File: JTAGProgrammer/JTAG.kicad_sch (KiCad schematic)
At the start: 27 parts, among them J2 878325623, J3 Conn_01x06, U4 74LVC3G17, U5 74LVC3G17

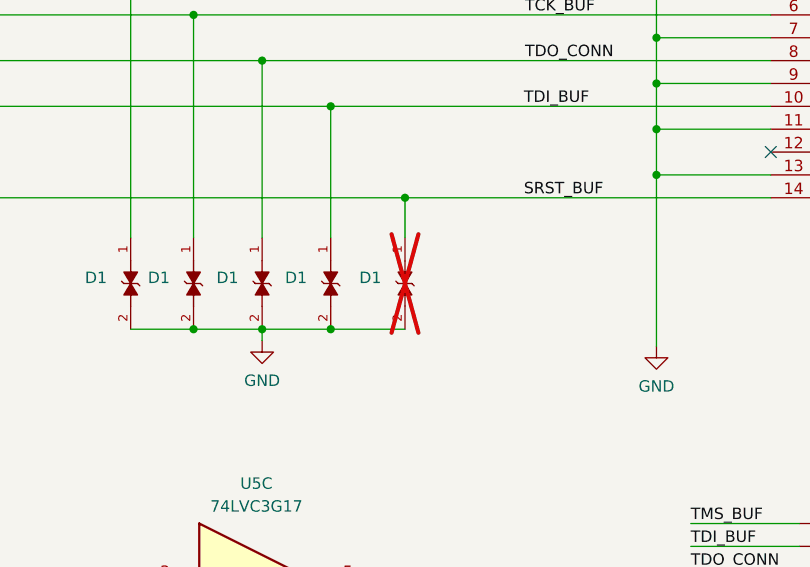
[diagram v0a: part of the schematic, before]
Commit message: Add LCSC part numbers
Signed-off-by: Anthony Bernaert <anthony.bernaert@gmail.com>
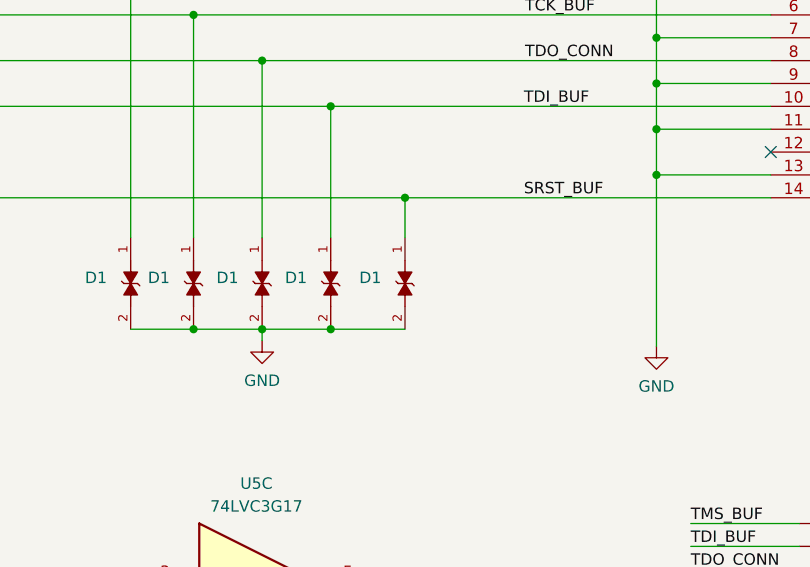
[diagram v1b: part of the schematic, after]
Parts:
- D1: LCSC (none) -> C142698
- D1: LCSC (none) -> C142698; now fitted; now in the parts list
- D4: LCSC (none) -> C324473
- J2: LCSC (none) -> C5197958
- J3: LCSC (none) -> C40877
- U4, U5: LCSC (none) -> C18213
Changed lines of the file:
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@@
+      (effects (font (size 1.27 1.27)) hide)
+    )
+    (property "LCSC" "C18213" (at 88.265 66.675 0)
       (effects (font (size 1.27 1.27)) hide)
     )
@@
     (property "Datasheet" "878325623" (at 237.49 47.625 0)
       (effects (font (size 1.27 1.27) italic) hide)
+    )
+    (property "LCSC" "C5197958" (at 237.49 47.625 0)
+      (effects (font (size 1.27 1.27)) hide)
     )
     (pin "1")
@@
       (effects (font (size 1.27 1.27)) hide)
     )
+    (property "LCSC" "C324473" (at 48.895 170.18 0)
+      (effects (font (size 1.27 1.27)) hide)
+    )
     (pin "1")
     (pin "2")
@@
     )
     (property "Datasheet" "http://www.ti.com/lit/sg/scyt129e/scyt129e.pdf" (at 87.63 104.14 0)
+      (effects (font (size 1.27 1.27)) hide)
+    )
+    (property "LCSC" "C18213" (at 87.63 104.14 0)
       (effects (font (size 1.27 1.27)) hide)
     )
@@
       (effects (font (size 1.27 1.27)) (justify bottom) hide)
     )
+    (property "LCSC" "C142698" (at 180.975 90.17 90)
+      (effects (font (size 1.27 1.27)) hide)
+    )
     (pin "1")
     (pin "2")
@@
     )
     (property "Datasheet" "http://www.ti.com/lit/sg/scyt129e/scyt129e.pdf" (at 87.63 121.92 0)
+      (effects (font (size 1.27 1.27)) hide)
+    )
+    (property "LCSC" "C18213" (at 87.63 121.92 0)
       (effects (font (size 1.27 1.27)) hide)
     )
@@
       (effects (font (size 1.27 1.27)) hide)
     )
+    (property "LCSC" "C18213" (at 85.725 83.82 0)
+      (effects (font (size 1.27 1.27)) hide)
+    )
     (pin "1")
     (pin "7")
@@
       (effects (font (size 1.27 1.27)) (justify bottom) hide)
     )
+    (property "LCSC" "C142698" (at 188.595 90.17 90)
+      (effects (font (size 1.27 1.27)) hide)
+    )
     (pin "1")
     (pin "2")
@@
     )
     (property "Datasheet" "http://www.ti.com/lit/sg/scyt129e/scyt129e.pdf" (at 88.265 48.895 0)
+      (effects (font (size 1.27 1.27)) hide)
+    )
+    (property "LCSC" "C18213" (at 88.265 48.895 0)
       (effects (font (size 1.27 1.27)) hide)
     )
@@
       (effects (font (size 1.27 1.27)) hide)
     )
+    (property "LCSC" "C18213" (at 113.03 164.465 0)
+      (effects (font (size 1.27 1.27)) hide)
+    )
     (pin "1")
     (pin "7")
@@
       (effects (font (size 1.27 1.27)) (justify bottom) hide)
     )
+    (property "LCSC" "C142698" (at 173.355 90.17 90)
+      (effects (font (size 1.27 1.27)) hide)
+    )
     (pin "1")
     (pin "2")
@@
     )
     (property "Datasheet" "http://www.ti.com/lit/sg/scyt129e/scyt129e.pdf" (at 127 164.465 0)
+      (effects (font (size 1.27 1.27)) hide)
+    )
+    (property "LCSC" "C18213" (at 127 164.465 0)
       (effects (font (size 1.27 1.27)) hide)
     )
@@
       (effects (font (size 1.27 1.27)) (justify bottom) hide)
     )
+    (property "LCSC" "C142698" (at 166.37 90.17 90)
+      (effects (font (size 1.27 1.27)) hide)
+    )
     (pin "1")
     (pin "2")
@@
     )
     (property "Datasheet" "http://www.ti.com/lit/sg/scyt129e/scyt129e.pdf" (at 181.61 123.19 0)
+      (effects (font (size 1.27 1.27)) hide)
+    )
+    (property "LCSC" "C18213" (at 181.61 123.19 0)
       (effects (font (size 1.27 1.27)) hide)
     )
@@
       (effects (font (size 1.27 1.27)) hide)
     )
+    (property "LCSC" "C40877" (at 245.745 121.92 0)
+      (effects (font (size 1.27 1.27)) hide)
+    )
     (pin "1")
     (pin "2")
@@
       (effects (font (size 1.27 1.27)) hide)
     )
+    (property "LCSC" "C324473" (at 48.895 147.955 0)
+      (effects (font (size 1.27 1.27)) hide)
+    )
     (pin "1")
     (pin "2")
@@
       (effects (font (size 1.27 1.27)) hide)
     )
+    (property "LCSC" "C324473" (at 48.26 158.75 0)
+      (effects (font (size 1.27 1.27)) hide)
+    )
     (pin "1")
     (pin "2")
@@
   )
   (symbol (lib_id "PGB1010603MR:PGB1010603MR") (at 196.85 90.17 270) (unit 1)
-    (in_bom no) (on_board yes) (dnp yes)
+    (in_bom yes) (on_board yes) (dnp no)
     (property "Reference" "D1" (at 191.77 89.535 90)
       (effects (font (size 1.27 1.27)) (justify left))
@@
       (effects (font (size 1.27 1.27)) (justify bottom) hide)
     )
-    (pin "1")
+    (property "LCSC" "C142698" (at 196.85 90.17 90)
+      (effects (font (size 1.27 1.27)) hide)
+    )
+    (pin "1")

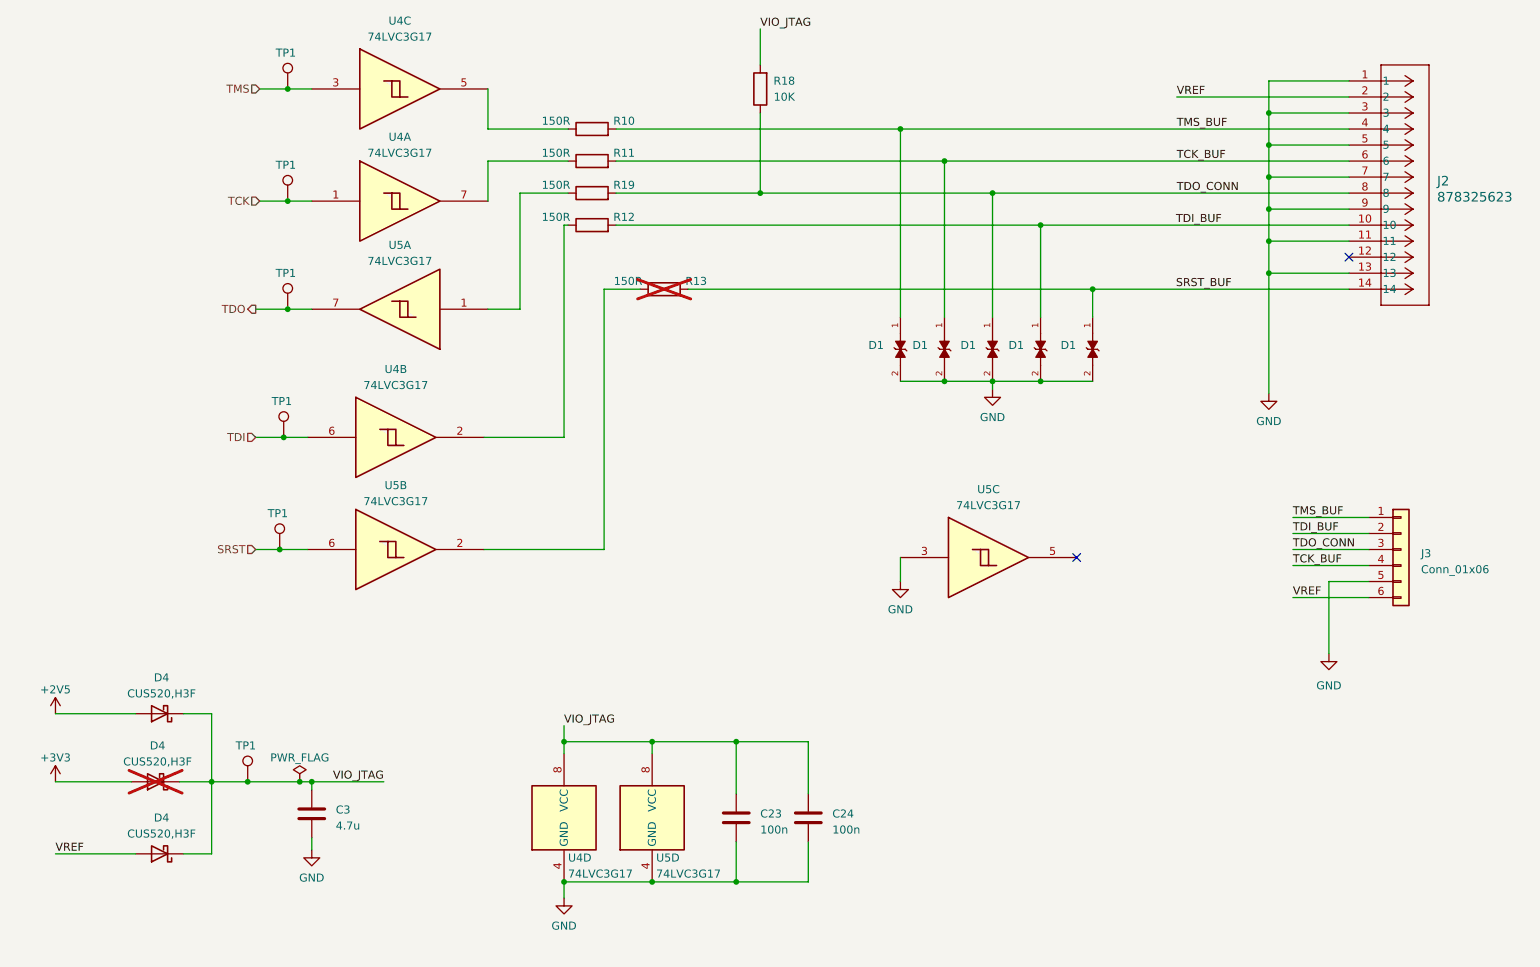
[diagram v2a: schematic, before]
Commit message: Rev.2: change to USB Type-C, add VBUS fuse, VREF LED indicators
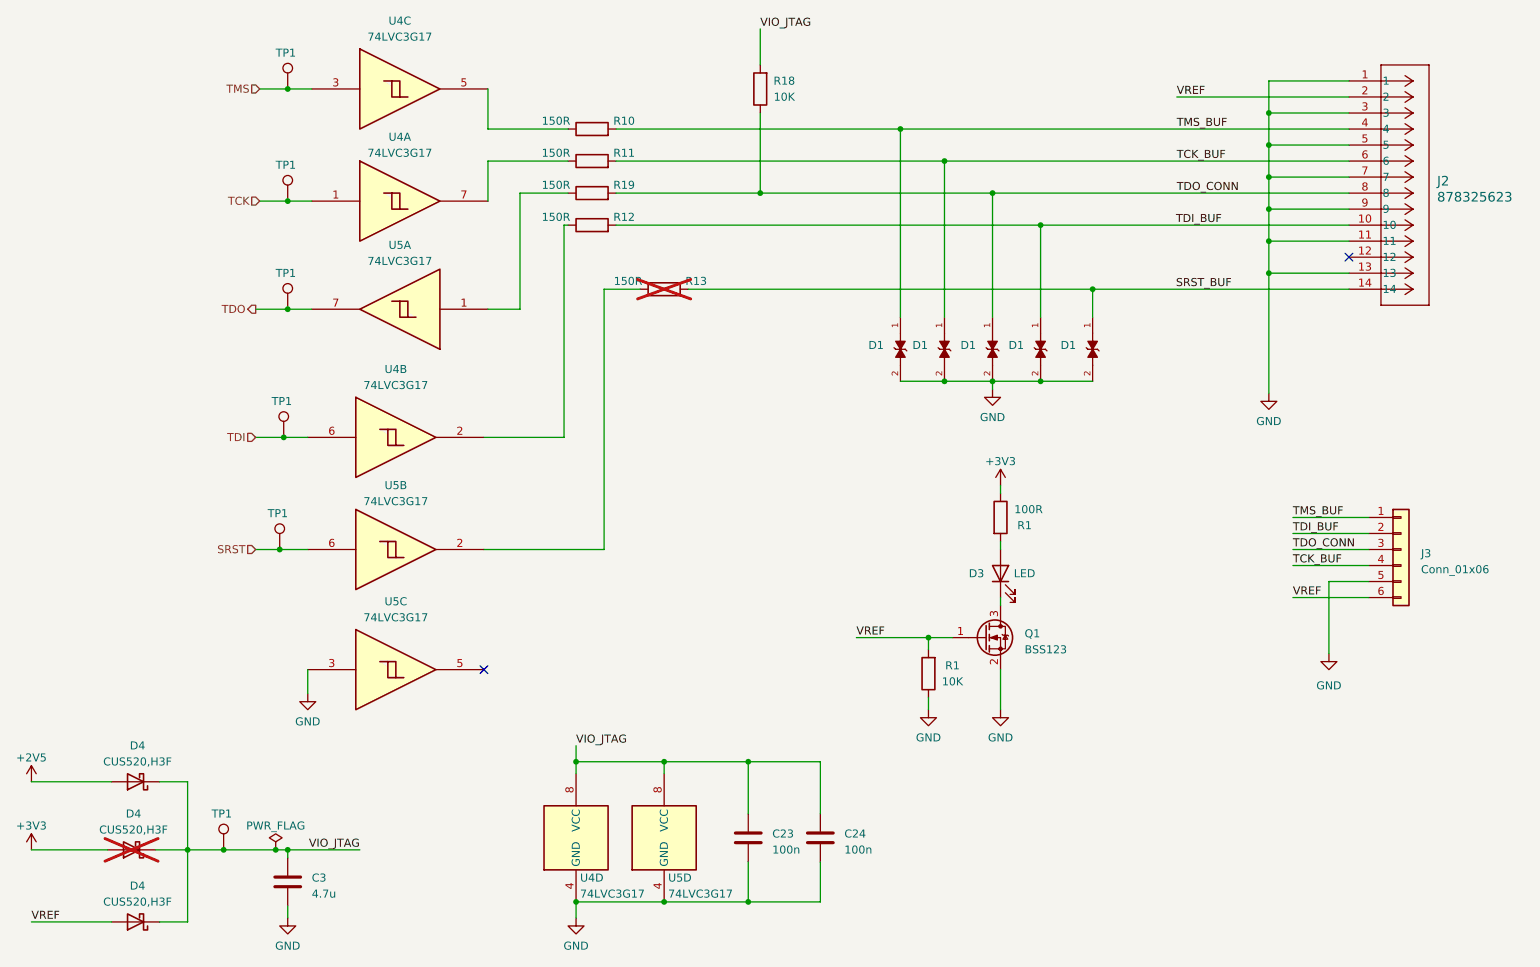
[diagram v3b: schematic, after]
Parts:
- added D3: LED, LED_SMD:LED_0603_1608Metric, symbol Device:LED
- added Q1: BSS123, Package_TO_SOT_SMD:SOT-23, symbol Transistor_FET:BSS123
- added R1: 10K, Resistor_SMD:R_0603_1608Metric, symbol Device:R
- added R1: 100R, Resistor_SMD:R_0603_1608Metric, symbol Device:R
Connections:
- net +3V3: now also R1.1
- net GND: now also Q1.2 (S), R1.1
- net VREF: now also Q1.1 (G), R1.2
- new net: D3.1 (K), Q1.3 (D)
- new net: D3.2 (A), R1.2
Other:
- moved on the sheet: C23, C24, C3, D4, TP1, U4D, U5C, U5D
